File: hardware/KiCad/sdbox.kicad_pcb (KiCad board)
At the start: 2 copper layers, 55 x 55.7 mm, 19 parts, among them J1 TO_PARALLEL_PORT, J3 Conn_01x01, J4 Conn_01x01, J5 Conn_01x01, J6 Conn_01x01, Q1 BC847BW, Q2 BC847BW, U1 Arduino_Nano_V3, U2 Micro_SD_Card_Module

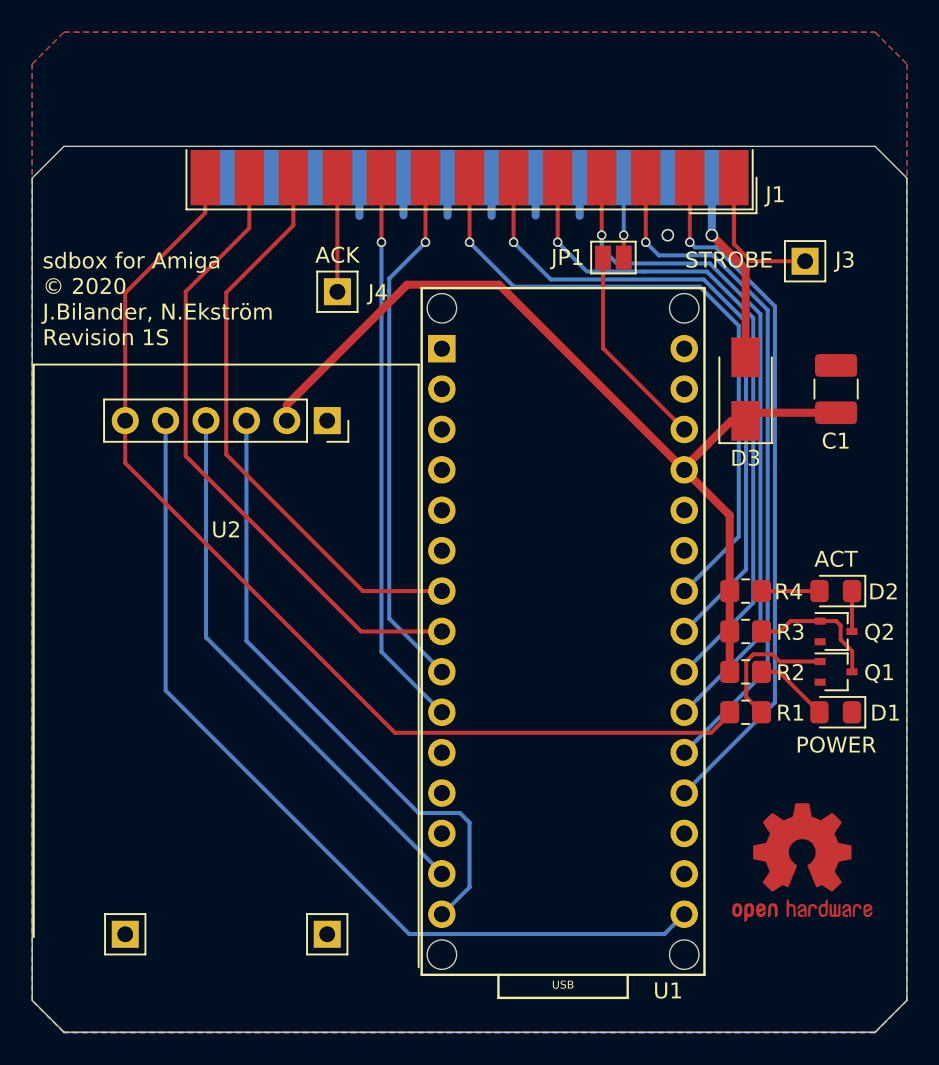
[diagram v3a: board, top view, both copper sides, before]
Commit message: Get back to protruding Nano and SD module
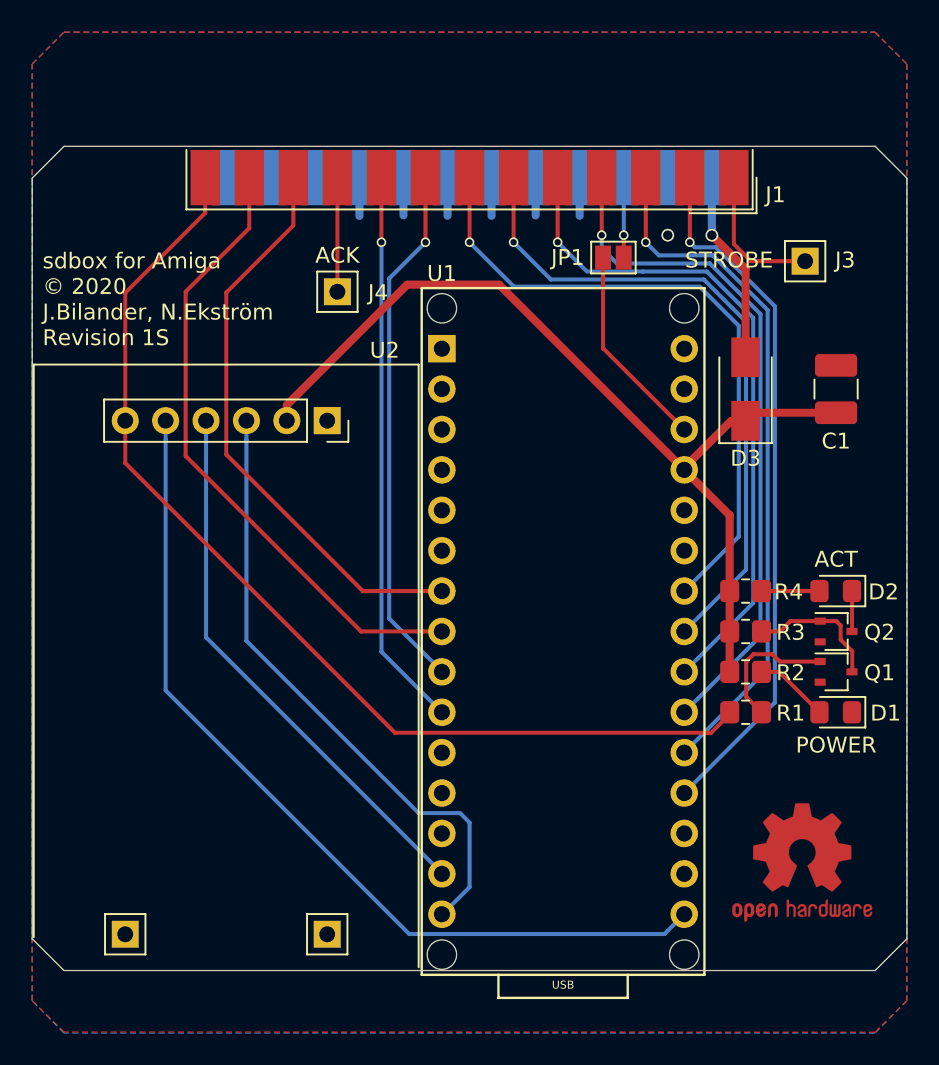
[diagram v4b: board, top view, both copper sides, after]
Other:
- board size 55 x 55.7 mm -> 55 x 51.8 mm
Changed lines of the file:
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@@
     (at 153.58 144.27)
     (descr https://store.arduino.cc/arduino-nano)
-    (fp_text reference U1 (at 6.604 1.016) (layer F.SilkS)
+    (fp_text reference U1 (at -7.62 -44.0935) (layer F.SilkS)
       (effects (font (size 1 1) (thickness 0.15)))
     )
     (fp_text value Arduino_Nano_V3 (at 0 -21.082 90) (layer F.Fab)
       (effects (font (size 1 1) (thickness 0.15)))
-    )
-    (fp_text user ICSP (at 0 -40.64) (layer F.Fab)
-      (effects (font (size 1 1) (thickness 0.15)))
-    )
-    (fp_text user 3.3V (at 6.35 -6.35 90) (layer F.SilkS) hide
-      (effects (font (size 0.5 0.5) (thickness 0.075)))
-    )
-    (fp_text user USB (at 0 0.635) (layer F.SilkS)
-      (effects (font (size 0.5 0.5) (thickness 0.075)))
     )
     (fp_line (start -8.89 -43.18) (end -8.89 0) (layer F.SilkS) (width 0.15))
@@
     (fp_circle (center 2.54 -39.37) (end 3.048 -39.37) (layer F.Fab) (width 0.15))
     (fp_circle (center 0 -39.37) (end 0.508 -39.37) (layer F.Fab) (width 0.15))
+    (fp_text user ICSP (at 0 -40.64) (layer F.Fab)
+      (effects (font (size 1 1) (thickness 0.15)))
+    )
+    (fp_text user 3.3V (at 6.35 -6.35 90) (layer F.SilkS) hide
+      (effects (font (size 0.5 0.5) (thickness 0.075)))
+    )
+    (fp_text user USB (at 0 0.635) (layer F.SilkS)
+      (effects (font (size 0.5 0.5) (thickness 0.075)))
+    )
     (pad "" np_thru_hole circle (at 7.62 -1.27) (size 1.85 1.85) (drill 1.85) (layers *.Cu *.Mask))
     (pad "" np_thru_hole circle (at -7.62 -1.27) (size 1.85 1.85) (drill 1.85) (layers *.Cu *.Mask))
@@
       (effects (font (size 1 1) (thickness 0.15)))
     )
-    (fp_text user %R (at 0 0) (layer F.Fab)
-      (effects (font (size 0.5 0.5) (thickness 0.08)))
-    )
     (fp_line (start 1 -0.6) (end -0.7 -0.6) (layer F.Fab) (width 0.1))
     (fp_line (start -0.7 -0.6) (end -1 -0.3) (layer F.Fab) (width 0.1))
@@
     (fp_line (start 1.85 -0.95) (end 1.85 0.95) (layer F.CrtYd) (width 0.05))
     (fp_line (start 1.85 0.95) (end -1.85 0.95) (layer F.CrtYd) (width 0.05))
+    (fp_text user %R (at 0 0) (layer F.Fab)
+      (effects (font (size 0.5 0.5) (thickness 0.08)))
+    )
     (pad 2 smd roundrect (at 1.025 0 180) (size 1.15 1.4) (layers F.Cu F.Paste F.Mask) (roundrect_rratio 0.217391)
       (net 21 "Net-(D2-Pad2)"))
@@
       (effects (font (size 1 1) (thickness 0.15)))
     )
-    (fp_text user %R (at 0 0) (layer F.Fab)
-      (effects (font (size 0.5 0.5) (thickness 0.08)))
-    )
     (fp_line (start -1 0.625) (end -1 -0.625) (layer F.Fab) (width 0.1))
     (fp_line (start -1 -0.625) (end 1 -0.625) (layer F.Fab) (width 0.1))
@@
     (fp_line (start 1.85 -0.95) (end 1.85 0.95) (layer F.CrtYd) (width 0.05))
     (fp_line (start 1.85 0.95) (end -1.85 0.95) (layer F.CrtYd) (width 0.05))
+    (fp_text user %R (at 0 0) (layer F.Fab)
+      (effects (font (size 0.5 0.5) (thickness 0.08)))
+    )
     (pad 2 smd roundrect (at 1 0 180) (size 1.2 1.4) (layers F.Cu F.Paste F.Mask) (roundrect_rratio 0.208333)
       (net 3 SELECT))
@@
     (fp_text value 4.7k (at 0 1.65) (layer F.Fab)
       (effects (font (size 1 1) (thickness 0.15)))
-    )
-    (fp_text user %R (at 0 0) (layer F.Fab)
-      (effects (font (size 0.5 0.5) (thickness 0.08)))
     )
     (fp_line (start -1 0.625) (end -1 -0.625) (layer F.Fab) (width 0.1))
@@
     (fp_line (start 1.85 -0.95) (end 1.85 0.95) (layer F.CrtYd) (width 0.05))
     (fp_line (start 1.85 0.95) (end -1.85 0.95) (layer F.CrtYd) (width 0.05))
+    (fp_text user %R (at 0 0) (layer F.Fab)
+      (effects (font (size 0.5 0.5) (thickness 0.08)))
+    )
     (pad 2 smd roundrect (at 1 0) (size 1.2 1.4) (layers F.Cu F.Paste F.Mask) (roundrect_rratio 0.208333)
       (net 22 "Net-(Q1-Pad3)"))
@@
     (descr "Through hole straight socket strip, 1x06, 2.54mm pitch, single row (from Kicad 4.0.7), script generated")
     (tags "Through hole socket strip THT 1x06 2.54mm single row")
-    (fp_text reference U2 (at 0 6.9 180) (layer F.SilkS)
+    (fp_text reference U2 (at 9.9615 -4.3975 180) (layer F.SilkS)
       (effects (font (size 1 1) (thickness 0.15)))
     )
@@
       (effects (font (size 1 1) (thickness 0.15)))
     )
-    (fp_text user %R (at 0 0 90) (layer F.Fab)
-      (effects (font (size 1 1) (thickness 0.15)))
-    )
     (fp_line (start -0.635 -1.27) (end 1.27 -1.27) (layer F.Fab) (width 0.1))
     (fp_line (start 1.27 -1.27) (end 1.27 1.27) (layer F.Fab) (width 0.1))
@@
     (fp_line (start 1.8 -1.8) (end -1.8 -1.8) (layer F.CrtYd) (width 0.05))
     (fp_line (start 1.27 -1.27) (end 1.27 1.27) (layer F.SilkS) (width 0.12))
+    (fp_text user %R (at 0 0 90) (layer F.Fab)
+      (effects (font (size 1 1) (thickness 0.15)))
+    )
     (pad 1 thru_hole rect (at 0 0) (size 1.7 1.7) (drill 1) (layers *.Cu *.Mask)
       (net 24 ACK))
@@
       (effects (font (size 1 1) (thickness 0.15)))
     )
-    (fp_text user %R (at 0 0 90) (layer F.Fab)
-      (effects (font (size 1 1) (thickness 0.15)))
-    )
     (fp_line (start -0.635 -1.27) (end 1.27 -1.27) (layer F.Fab) (width 0.1))
     (fp_line (start 1.27 -1.27) (end 1.27 1.27) (layer F.Fab) (width 0.1))
@@
     (fp_line (start 1.8 -1.8) (end -1.8 -1.8) (layer F.CrtYd) (width 0.05))
     (fp_line (start 1.27 -1.27) (end 1.27 1.27) (layer F.SilkS) (width 0.12))
+    (fp_text user %R (at 0 0 90) (layer F.Fab)
+      (effects (font (size 1 1) (thickness 0.15)))
+    )
     (pad 1 thru_hole rect (at 0 0) (size 1.7 1.7) (drill 1) (layers *.Cu *.Mask))
     (model ${KISYS3DMOD}/Connector_PinHeader_2.54mm.3dshapes/PinHeader_1x01_P2.54mm_Vertical.wrl
@@
     (effects (font (size 1 1) (thickness 0.2)) (justify left))
   )
-  (gr_line (start 120.2 145.8735) (end 122.2 147.8735) (layer Edge.Cuts) (width 0.05))
-  (gr_line (start 175.2 145.8735) (end 173.2 147.8735) (layer Edge.Cuts) (width 0.05))
+  (gr_line (start 120.2 142) (end 122.2 144) (layer Edge.Cuts) (width 0.05))
+  (gr_line (start 175.2 142) (end 173.2 144) (layer Edge.Cuts) (width 0.05))
   (gr_line (start 173.2 92.1755) (end 175.2 94.1755) (layer Edge.Cuts) (width 0.05))
   (gr_line (start 120.2 94.1755) (end 122.2 92.1755) (layer Edge.Cuts) (width 0.05))
-  (gr_line (start 120.2 94.1755) (end 120.2 145.8735) (layer Edge.Cuts) (width 0.05))
-  (gr_line (start 122.2 147.8735) (end 173.2 147.8735) (layer Edge.Cuts) (width 0.05))
-  (gr_line (start 175.2 94.1755) (end 175.2 145.8735) (layer Edge.Cuts) (width 0.05))
+  (gr_line (start 120.2 94.1755) (end 120.2 142) (layer Edge.Cuts) (width 0.05))
+  (gr_line (start 122.2 144) (end 173.2 144) (layer Edge.Cuts) (width 0.05))
+  (gr_line (start 175.2 94.1755) (end 175.2 142) (layer Edge.Cuts) (width 0.05))
   (gr_line (start 122.2 92.1755) (end 173.2 92.1755) (layer Edge.Cuts) (width 0.05))
   (segment (start 140.775 94.144) (end 140.775 96.556) (width 0.508) (layer B.Cu) (net 1))
@@
   (segment (start 165.0555 99.884) (end 165.0555 105.44) (width 0.508) (layer F.Cu) (net 19))
   (segment (start 162.935 97.7635) (end 165.0555 99.884) (width 0.508) (layer F.Cu) (net 19))
-  (segment (start 166.0555 120.14) (end 169.6985 120.14) (width 0.254) (layer F.Cu) (net 21))
-  (segment (start 171.7485 122.6775) (end 171.746 122.68) (width 0.254) (layer F.Cu) (net 26))
-  (segment (start 171.7485 120.14) (end 171.7485 122.6775) (width 0.254) (layer F.Cu) (net 26))
   (segment (start 167.1585 125.22) (end 169.6985 127.76) (width 0.254) (layer F.Cu) (net 20))
   (segment (start 166.0555 125.22) (end 167.1585 125.22) (width 0.254) (layer F.Cu) (net 20))
+  (segment (start 166.0555 120.14) (end 169.6985 120.14) (width 0.254) (layer F.Cu) (net 21))
   (segment (start 166.0555 122.68) (end 167.229 122.68) (width 0.254) (layer F.Cu) (net 22))
   (segment (start 167.879 122.03) (end 169.746 122.03) (width 0.254) (layer F.Cu) (net 22))
@@
   (segment (start 164.32 98.3225) (end 165.3975 99.4) (width 0.254) (layer F.Cu) (net 25))
   (segment (start 164.32 94.144) (end 164.32 98.3225) (width 0.254) (layer F.Cu) (net 25))
+  (segment (start 171.7485 122.6775) (end 171.746 122.68) (width 0.254) (layer F.Cu) (net 26))
+  (segment (start 171.7485 120.14) (end 171.7485 122.6775) (width 0.254) (layer F.Cu) (net 26))
   (zone (net 1) (net_name GND) (layer F.Cu) (hatch edge 0.508)
     (connect_pads (clearance 0.1))
     (min_thickness 0.254)
-    (fill (arc_segments 32) (thermal_gap 0.254) (thermal_bridge_width 0.508))
+    (fill yes (arc_segments 32) (thermal_gap 0.254) (thermal_bridge_width 0.508))
     (polygon
       (pts
@@
     (connect_pads (clearance 0.1))
     (min_thickness 0.254)
-    (fill (arc_segments 32) (thermal_gap 0.254) (thermal_bridge_width 0.508))
+    (fill yes (arc_segments 32) (thermal_gap 0.254) (thermal_bridge_width 0.508))
     (polygon
       (pts

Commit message: Use SOT-23 BJTs
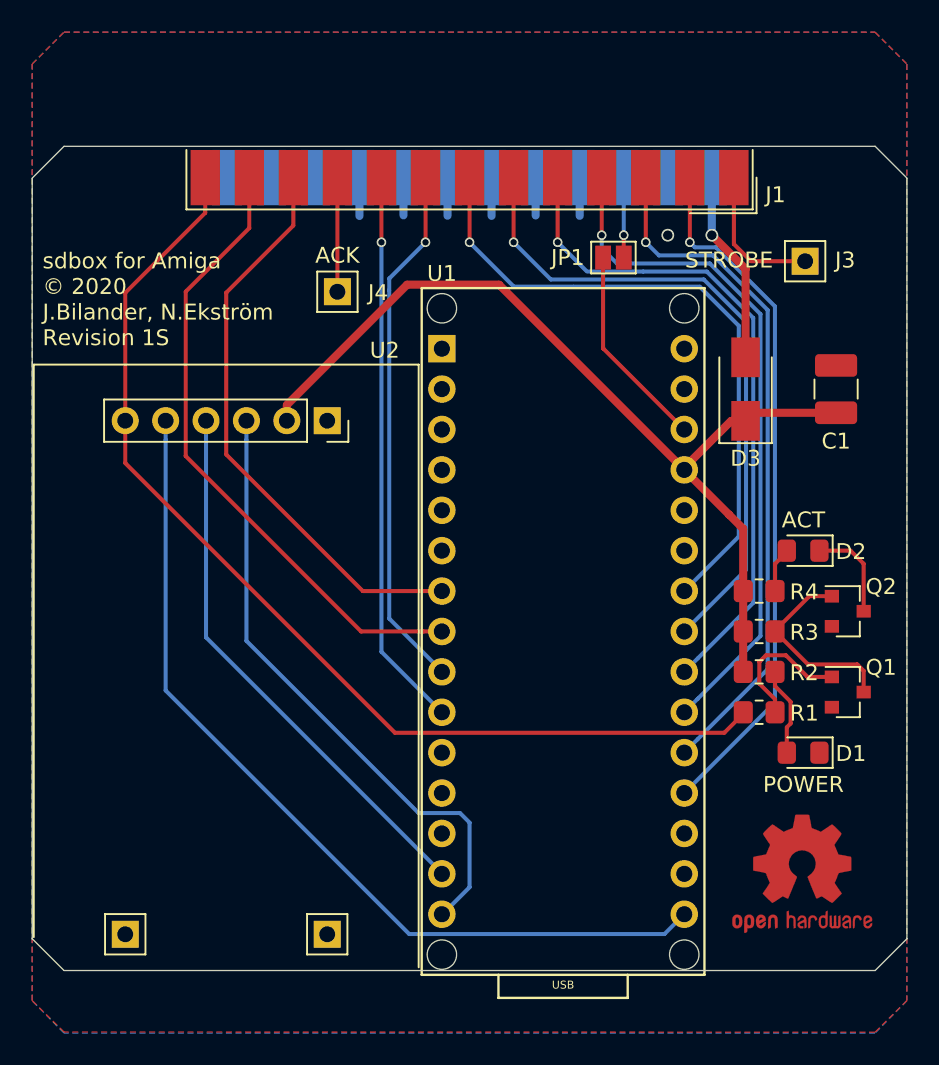
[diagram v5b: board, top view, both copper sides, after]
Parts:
- Q1, Q2: footprint Package_TO_SOT_SMD:SOT-323_SC-70 -> Package_TO_SOT_SMD:SOT-23
- moved D1 3.27 mm to (168.7, 130.3)
- moved D2 3.27 mm to (168.7, 117.6)
- moved Q1 1.47 mm to (171.5, 126.5)
- moved Q2 1.47 mm to (171.5, 121.4)
- moved R1 0.85 mm to (165.9, 127.8)
- moved R2 0.85 mm to (165.9, 125.2)
- moved R3 0.85 mm to (165.9, 122.7)
- moved R4 0.85 mm to (165.9, 120.1)
- moved V0 0.71 mm to (168.6, 137.9)
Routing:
- net Net-(Q1-Pad3): track 8.79 -> 12.5 mm
- net Net-(D2-Pad1): track 2.54 -> 6.11 mm
- net Net-(D1-Pad2): track 4.70 -> 5.59 mm
- net SELECT: track 65.7 -> 66.5 mm
- net Net-(D2-Pad2): track 3.64 -> 2.85 mm
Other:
- rule pad_to_mask_clearance: 0.051 -> 0

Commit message: Minor tweaks
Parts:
- U1: footprint Arduino:Arduino_Nano_Socket -> SDBox:Arduino_Nano_Socket
- moved D3 0.85 mm to (165.9, 107.4)
- moved C1 0.73 mm to (171.5, 107.4)
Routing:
- net 5V: track 59.3 -> 60.0 mm

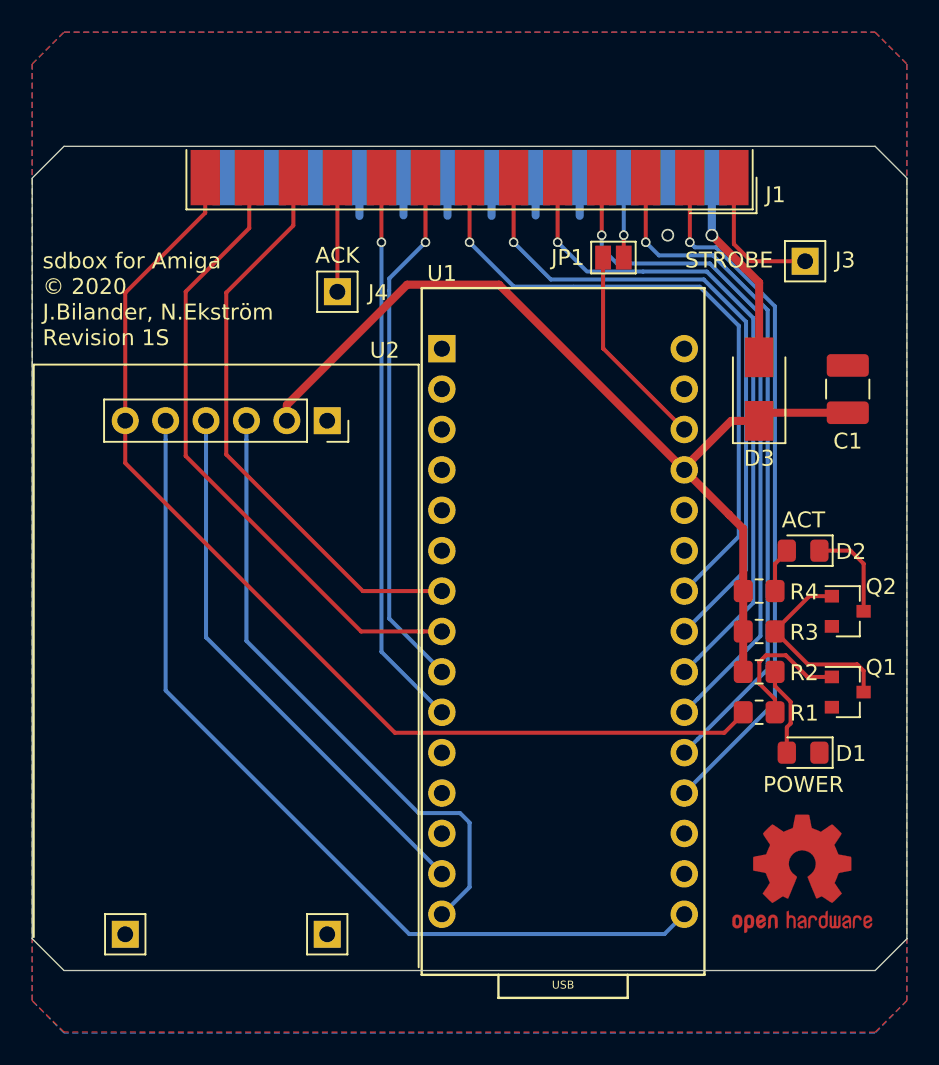
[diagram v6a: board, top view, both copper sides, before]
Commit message: Add pin names on silkscreen
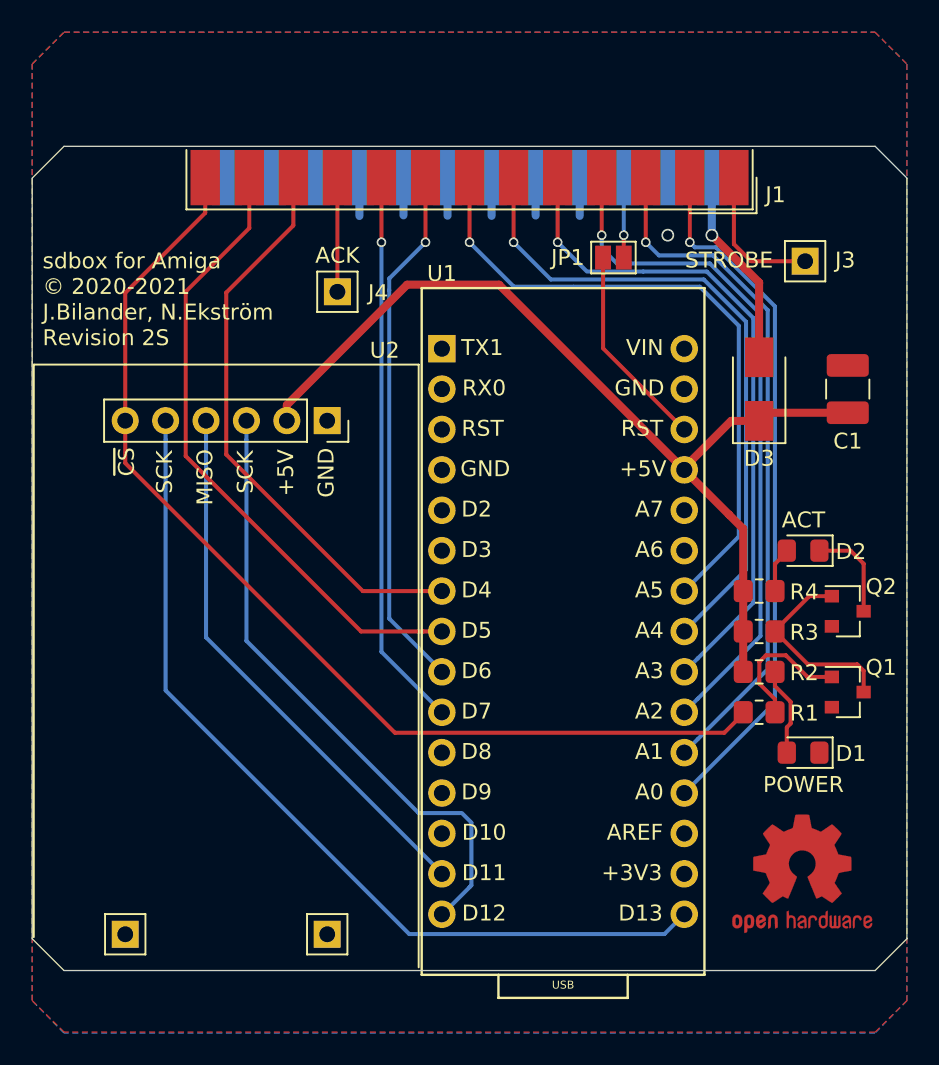
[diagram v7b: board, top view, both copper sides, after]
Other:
- board text added: "+3V3"
- board text added: "+5V"
- board text added: "A0"
- board text added: "A1"
- board text added: "A2"
- board text added: "A3"
- board text added: "A4"
- board text added: "A5"
- board text added: "A6"
- board text added: "A7"
- board text added: "AREF"
- board text added: "D10"
- board text added: "D11"
- board text added: "D12"
- board text added: "D13"
- board text added: "D2"
- board text added: "D3"
- board text added: "D4"
- board text added: "D5"
- board text added: "D6"
- board text added: "D7"
- board text added: "D8"
- board text added: "D9"
- board text added: "GND"
- board text added: "MISO"
- board text added: "RST"
- board text added: "RX0"
- board text added: "SCK"
- board text added: "TX1"
- board text added: "VIN"
- board text added: "sdbox for Amiga © 2020-2021 J.Bilander, N.Ekström Revision 2S"
- board text added: "~CS"
- board text removed: "sdbox for Amiga © 2020 J.Bilander, N.Ekström Revision 1S"
